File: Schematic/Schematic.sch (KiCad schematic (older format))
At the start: 35 parts, among them M1 Motor_DC, M2 Motor_DC, SW1 SW, U1 L7805

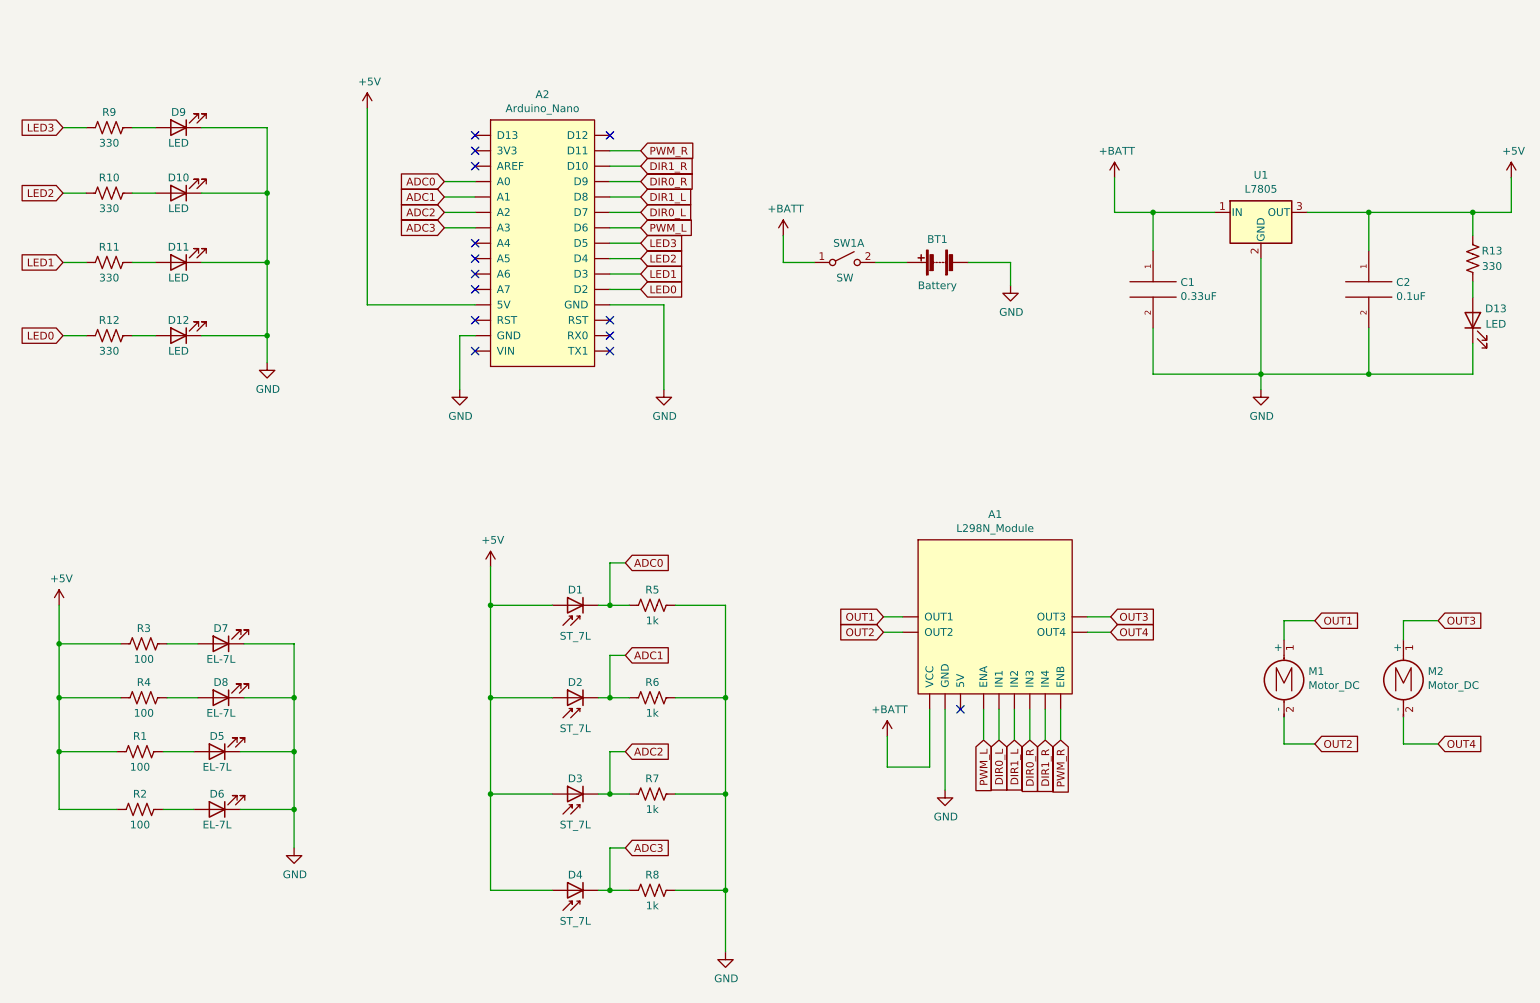
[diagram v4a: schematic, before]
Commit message: Update Schematic
- global label에서 net label로 수정
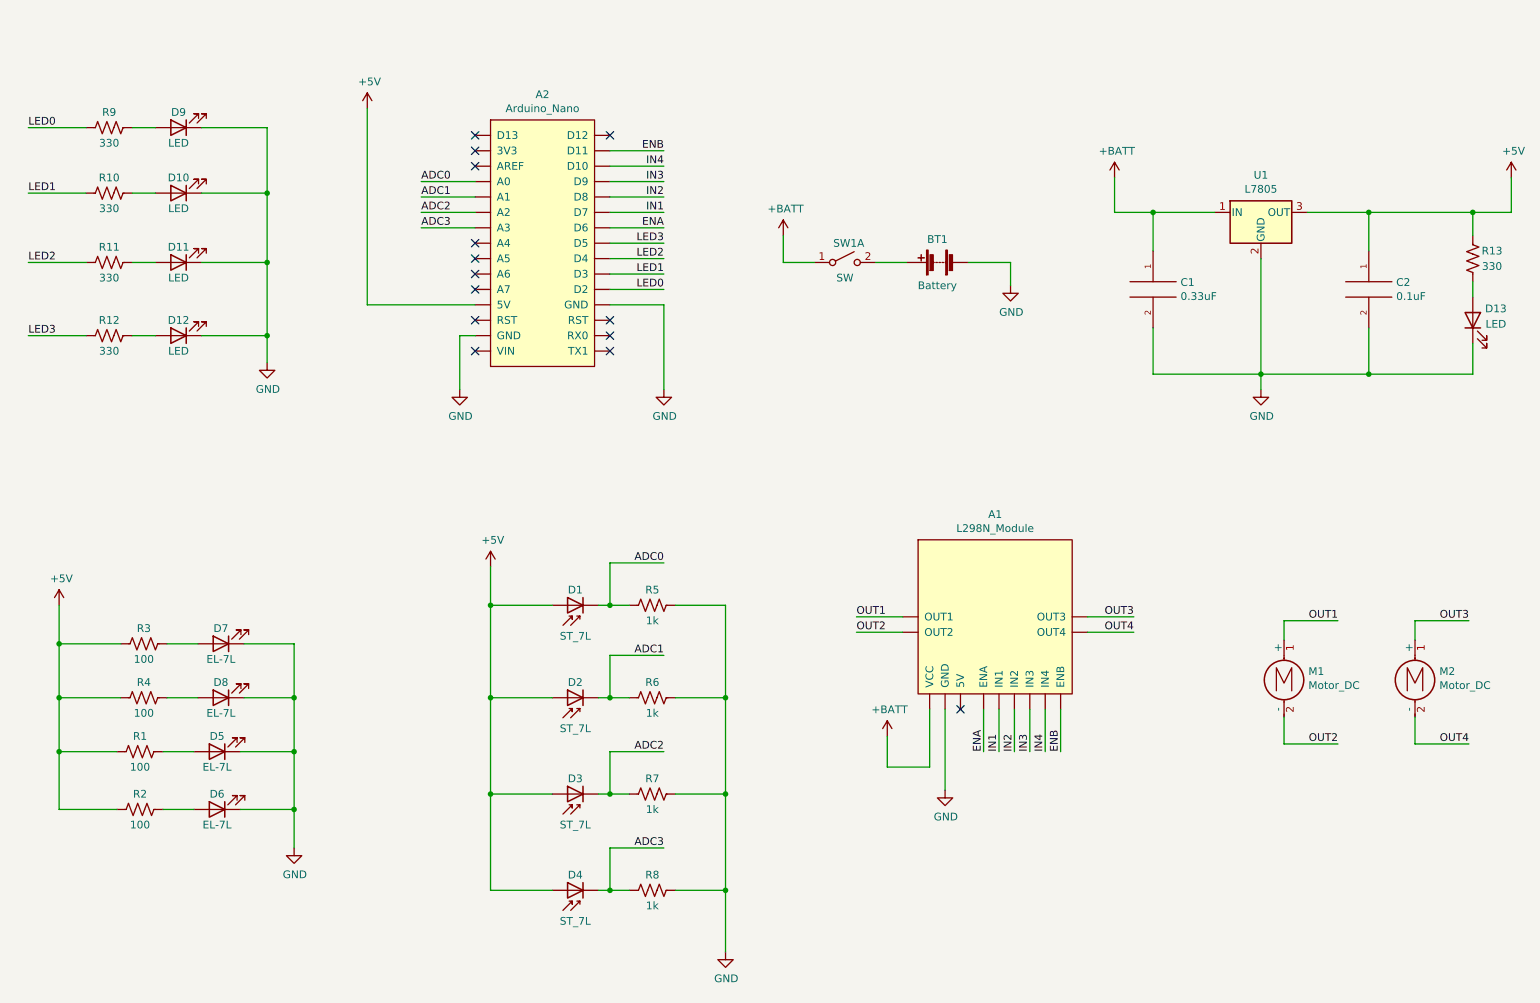
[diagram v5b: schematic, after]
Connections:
- net LED0: now also R9.2; no longer R12.2
- net LED1: now also R10.2; no longer R11.2
- net LED2: now also R11.2; no longer R10.2
- net LED3: now also R12.2; no longer R9.2
- removed net DIR0_L: A1.~ (VCC), A2.~ (VIN)
- removed net DIR0_R: A1.~ (VCC), A2.~ (VIN)
- removed net DIR1_L: A1.~ (VCC), A2.~ (VIN)
- removed net DIR1_R: A1.~ (VCC), A2.~ (VIN)
- removed net PWM_L: A1.~ (VCC), A2.~ (VIN)
- removed net PWM_R: A1.~ (VCC), A2.~ (VIN)
- new net ENA: A1.~ (VCC), A2.~ (VIN)
- new net ENB: A1.~ (VCC), A2.~ (VIN)
- new net IN1: A1.~ (VCC), A2.~ (VIN)
- new net IN2: A1.~ (VCC), A2.~ (VIN)
- new net IN3: A1.~ (VCC), A2.~ (VIN)
- new net IN4: A1.~ (VCC), A2.~ (VIN)
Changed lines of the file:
@@
 	1    0    0    -1
 $EndComp
-Text GLabel 4975 2700 2    50   Input ~ 0
-LED0
-Text GLabel 4975 2600 2    50   Input ~ 0
-LED1
-Text GLabel 4975 2500 2    50   Input ~ 0
-LED2
-Text GLabel 4975 2400 2    50   Input ~ 0
-LED3
-Wire Wire Line
-	4775 2700 4975 2700
-Wire Wire Line
-	4775 2600 4975 2600
-Wire Wire Line
-	4775 2500 4975 2500
-Wire Wire Line
-	4775 2400 4975 2400
-Text GLabel 1225 1650 0    50   Input ~ 0
-LED3
+Wire Wire Line
+	4775 2700 5125 2700
 $Comp
 L Device:LED D9
@@
 $EndComp
 Wire Wire Line
-	1225 1650 1375 1650
+	1000 1650 1375 1650
 Wire Wire Line
 	1675 1650 1825 1650
-Text GLabel 1225 2075 0    50   Input ~ 0
-LED2
 $Comp
 L Device:LED D10
@@
 $EndComp
 Wire Wire Line
-	1225 2075 1375 2075
-Wire Wire Line
 	1675 2075 1825 2075
-Text GLabel 1225 2525 0    50   Input ~ 0
-LED1
 $Comp
 L Device:LED D11
@@
 $EndComp
 Wire Wire Line
-	1225 2525 1375 2525
-Wire Wire Line
 	1675 2525 1825 2525
-Text GLabel 1225 3000 0    50   Input ~ 0
-LED0
 $Comp
 L Device:LED D12
@@
 $EndComp
 Wire Wire Line
-	1225 3000 1375 3000
-Wire Wire Line
 	1675 3000 1825 3000
 Wire Wire Line
@@
 	0    1    1    0
 $EndComp
-Text GLabel 7400 5625 3    50   Input ~ 0
-DIR1_L
-Wire Wire Line
-	7400 5425 7400 5625
-Text GLabel 7300 5625 3    50   Input ~ 0
-DIR0_L
-Wire Wire Line
-	7300 5425 7300 5625
-Text GLabel 7500 5625 3    50   Input ~ 0
-DIR0_R
-Wire Wire Line
-	7500 5425 7500 5625
-Text GLabel 7600 5625 3    50   Input ~ 0
-DIR1_R
-Wire Wire Line
-	7600 5425 7600 5625
-Wire Wire Line
-	4775 2200 4975 2200
-Wire Wire Line
-	4775 2300 4975 2300
-Wire Wire Line
-	4775 2100 4975 2100
-Wire Wire Line
-	4775 2000 4975 2000
-Wire Wire Line
-	7200 5425 7200 5625
-Wire Wire Line
-	7700 5425 7700 5625
-Wire Wire Line
-	4775 1900 4975 1900
-Wire Wire Line
-	4775 1800 4975 1800
-Text GLabel 9350 4850 2    50   Input ~ 0
-OUT1
-Text GLabel 6550 4825 0    50   Input ~ 0
-OUT1
-Wire Wire Line
-	6550 4825 6675 4825
+Wire Wire Line
+	7400 5425 7400 5700
+Wire Wire Line
+	7300 5425 7300 5700
+Wire Wire Line
+	7500 5425 7500 5700
+Wire Wire Line
+	7600 5425 7600 5700
+Wire Wire Line
+	7200 5425 7200 5700
+Wire Wire Line
+	7700 5425 7700 5700
+Wire Wire Line
+	6375 4825 6675 4825
 Wire Wire Line
 	9150 4975 9150 4850
 Wire Wire Line
-	9150 4850 9350 4850
-Text GLabel 6550 4925 0    50   Input ~ 0
-OUT2
-Wire Wire Line
-	6550 4925 6675 4925
-Text GLabel 9350 5650 2    50   Input ~ 0
-OUT2
+	9150 4850 9500 4850
+Wire Wire Line
+	6375 4925 6675 4925
 Wire Wire Line
 	9150 5475 9150 5650
 Wire Wire Line
-	9150 5650 9350 5650
-$Comp
-L Motor:Motor_DC M2
-U 1 1 61F968A7
-P 9925 5175
-F 0 "M2" H 10083 5171 50  0000 L CNN
-F 1 "Motor_DC" H 10083 5080 50  0000 L CNN
-F 2 "" H 9925 5085 50  0001 C CNN
-F 3 "~" H 9925 5085 50  0001 C CNN
-	1    9925 5175
-	1    0    0    -1
-$EndComp
-Text GLabel 10150 4850 2    50   Input ~ 0
-OUT3
-Wire Wire Line
-	9925 4975 9925 4850
-Wire Wire Line
-	9925 4850 10150 4850
-Text GLabel 10150 5650 2    50   Input ~ 0
-OUT4
-Wire Wire Line
-	9925 5475 9925 5650
-Wire Wire Line
-	9925 5650 10150 5650
-Text GLabel 8025 4825 2    50   Input ~ 0
-OUT3
-Text GLabel 8025 4925 2    50   Input ~ 0
-OUT4
-Wire Wire Line
-	7875 4825 8025 4825
-Wire Wire Line
-	7875 4925 8025 4925
+	9150 5650 9500 5650
 $Comp
 L power:GND #PWR08
@@
 	-1   0    0    1
 $EndComp
-Text GLabel 3700 2000 0    50   Input ~ 0
-ADC0
-Wire Wire Line
-	3700 2000 3900 2000
-Text GLabel 3700 2100 0    50   Input ~ 0
-ADC1
-Wire Wire Line
-	3700 2100 3900 2100
-Text GLabel 3700 2200 0    50   Input ~ 0
-ADC2
-Wire Wire Line
-	3700 2200 3900 2200
-Text GLabel 3700 2300 0    50   Input ~ 0
-ADC3
-Wire Wire Line
-	3700 2300 3900 2300
+Wire Wire Line
+	3550 2100 3900 2100
+Wire Wire Line
+	3550 2200 3900 2200
+Wire Wire Line
+	3550 2300 3900 2300
 $Comp
 L power:+5V #PWR06
@@
 NoConn ~ 3900 2700
 NoConn ~ 3900 2900
-Text GLabel 7200 5625 3    50   Input ~ 0
-PWM_L
-Text GLabel 7700 5625 3    50   Input ~ 0
-PWM_R
-Text GLabel 4975 2100 2    50   Input ~ 0
-DIR1_L
-Text GLabel 4975 2200 2    50   Input ~ 0
-DIR0_L
-Text GLabel 4975 2000 2    50   Input ~ 0
-DIR0_R
-Text GLabel 4975 1900 2    50   Input ~ 0
-DIR1_R
-Text GLabel 4975 2300 2    50   Input ~ 0
-PWM_L
-Text GLabel 4975 1800 2    50   Input ~ 0
-PWM_R
 Wire Wire Line
 	2550 1650 2550 2075
@@
 $EndComp
 Wire Wire Line
-	8300 2200 8300 2450
-Wire Wire Line
 	8300 2200 8700 2200
 Wire Wire Line
@@
 	9700 3250 9000 3250
 $Comp
-L power:+BATT #PWR05
-U 1 1 620070BA
-P 8050 1975
-F 0 "#PWR05" H 8050 1825 50  0001 C CNN
-F 1 "+BATT" H 8065 2148 50  0000 C CNN
-F 2 "" H 8050 1975 50  0001 C CNN
-F 3 "" H 8050 1975 50  0001 C CNN
-	1    8050 1975
-	1    0    0    -1
-$EndComp
-Wire Wire Line
-	8050 1975 8050 2200
-$Comp
 L power:+5V #PWR013
 U 1 1 6200C7B2
@@
 	1    0    0    -1
 $EndComp
-Text GLabel 4875 5700 2    50   Input ~ 0
-ADC2
-Wire Wire Line
-	4875 5700 4775 5700
+Wire Wire Line
+	5125 5700 4775 5700
 Wire Wire Line
 	5525 6600 5525 7000
@@
 	4775 6325 4775 6600
 Wire Wire Line
-	4875 6325 4775 6325
-Text GLabel 4875 6325 2    50   Input ~ 0
-ADC3
+	5125 6325 4775 6325
 Wire Wire Line
 	5200 6600 5525 6600
@@
 	4775 5075 4775 5350
 Wire Wire Line
-	4875 5075 4775 5075
-Text GLabel 4875 5075 2    50   Input ~ 0
-ADC1
+	5125 5075 4775 5075
 Wire Wire Line
 	5200 5350 5525 5350
@@
 	4775 4475 4775 4750
 Wire Wire Line
-	4875 4475 4775 4475
-Text GLabel 4875 4475 2    50   Input ~ 0
-ADC0
+	5125 4475 4775 4475
 Wire Wire Line
 	5200 4750 5525 4750
@@
 Wire Wire Line
 	5900 2525 6100 2525
+Text Label 3550 2000 0    50   ~ 0
+ADC0
+Wire Wire Line
+	3550 2000 3900 2000
+Text Label 3550 2100 0    50   ~ 0
+ADC1
+Text Label 3550 2200 0    50   ~ 0
+ADC2
+Text Label 3550 2300 0    50   ~ 0
+ADC3
+Text Label 5125 4475 2    50   ~ 0
+ADC0
+Text Label 5125 5075 2    50   ~ 0
+ADC1
+Text Label 5125 5700 2    50   ~ 0
+ADC2
+Text Label 5125 6325 2    50   ~ 0
+ADC3
+Wire Wire Line
+	8300 2200 8300 2450
 Wire Wire Line
 	8050 2200 8300 2200
+$Comp
+L power:+BATT #PWR05
+U 1 1 620070BA
+P 8050 1975
+F 0 "#PWR05" H 8050 1825 50  0001 C CNN
+F 1 "+BATT" H 8065 2148 50  0000 C CNN
+F 2 "" H 8050 1975 50  0001 C CNN
+F 3 "" H 8050 1975 50  0001 C CNN
+	1    8050 1975
+	1    0    0    -1
+$EndComp
+Wire Wire Line
+	8050 1975 8050 2200
+Text Label 6375 4825 0    50   ~ 0
+OUT1
+Text Label 6375 4925 0    50   ~ 0
+OUT2
+Wire Wire Line
+	8175 4925 7875 4925
+Wire Wire Line
+	8175 4825 7875 4825
+Text Label 8175 4925 2    50   ~ 0
+OUT4
+Text Label 8175 4825 2    50   ~ 0
+OUT3
+Text Label 9500 4850 2    50   ~ 0
+OUT1
+Text Label 9500 5650 2    50   ~ 0
+OUT2
+$Comp
+L Motor:Motor_DC M2
+U 1 1 6207D101
+P 10000 5175
+F 0 "M2" H 10158 5171 50  0000 L CNN
+F 1 "Motor_DC" H 10158 5080 50  0000 L CNN
+F 2 "" H 10000 5085 50  0001 C CNN
+F 3 "~" H 10000 5085 50  0001 C CNN
+	1    10000 5175
+	1    0    0    -1
+$EndComp
+Wire Wire Line
+	10000 4975 10000 4850
+Wire Wire Line
+	10000 4850 10350 4850
+Wire Wire Line
+	10000 5475 10000 5650
+Wire Wire Line
+	10000 5650 10350 5650
+Text Label 10350 4850 2    50   ~ 0
+OUT3
+Text Label 10350 5650 2    50   ~ 0
+OUT4
+Text Label 1000 1650 0    50   ~ 0
+LED0
+Wire Wire Line
+	1000 2075 1375 2075
+Text Label 1000 2075 0    50   ~ 0
+LED1
+Wire Wire Line
+	1000 2525 1375 2525
+Text Label 1000 2525 0    50   ~ 0
+LED2
+Wire Wire Line
+	1000 3000 1375 3000
+Text Label 1000 3000 0    50   ~ 0
+LED3
+Text Label 5125 2700 2    50   ~ 0
+LED0
+Wire Wire Line
+	4775 2600 5125 2600
+Text Label 5125 2600 2    50   ~ 0
+LED1
+Wire Wire Line
+	4775 2400 5125 2400
+Text Label 5125 2400 2    50   ~ 0
+LED3
+Wire Wire Line
+	4775 2500 5125 2500
+Text Label 5125 2500 2    50   ~ 0
+LED2
+Text Label 7200 5700 1    50   ~ 0
+ENA
+Text Label 7300 5700 1    50   ~ 0
+IN1
+Text Label 7400 5700 1    50   ~ 0
+IN2
+Text Label 7500 5700 1    50   ~ 0
+IN3
+Text Label 7600 5700 1    50   ~ 0
+IN4
+Text Label 7700 5700 1    50   ~ 0
+ENB
+Text Label 5125 1800 2    50   ~ 0
+ENB
+Text Label 5125 1900 2    50   ~ 0
+IN4
+Text Label 5125 2000 2    50   ~ 0
+IN3
+Text Label 5125 2100 2    50   ~ 0
+IN2
+Text Label 5125 2200 2    50   ~ 0
+IN1
+Text Label 5125 2300 2    50   ~ 0
+ENA
+Wire Wire Line
+	4775 1800 5125 1800
+Wire Wire Line
+	4775 2300 5125 2300
+Wire Wire Line
+	4775 1900 5125 1900
+Wire Wire Line
+	4775 2000 5125 2000
+Wire Wire Line
+	4775 2200 5125 2200
+Wire Wire Line
+	4775 2100 5125 2100
 $EndSCHEMATC
